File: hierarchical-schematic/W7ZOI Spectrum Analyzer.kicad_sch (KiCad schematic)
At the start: 2 parts

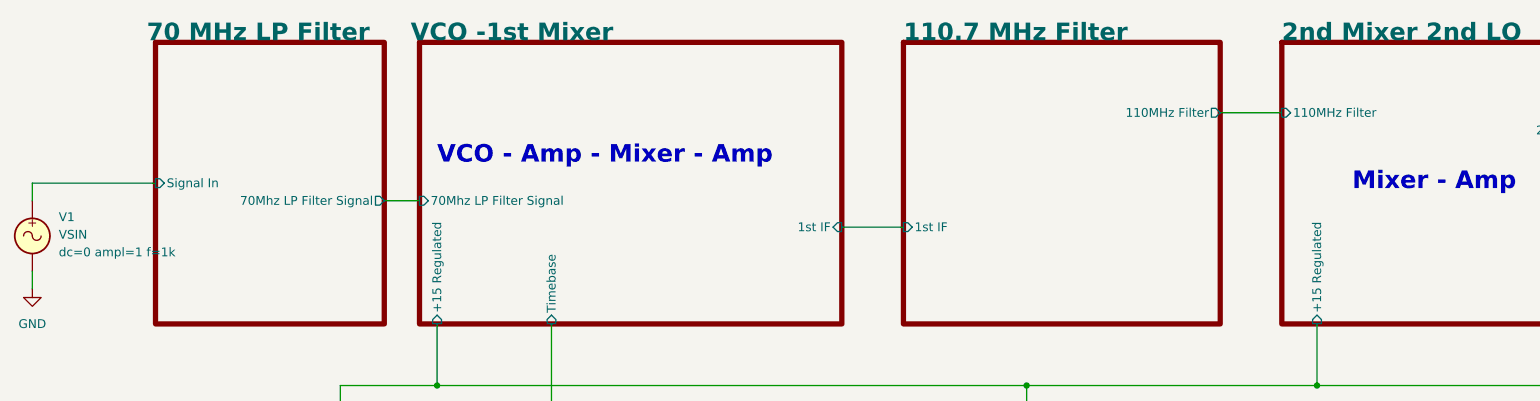
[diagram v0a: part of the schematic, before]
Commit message: Update to timebase and 2lo gerbers
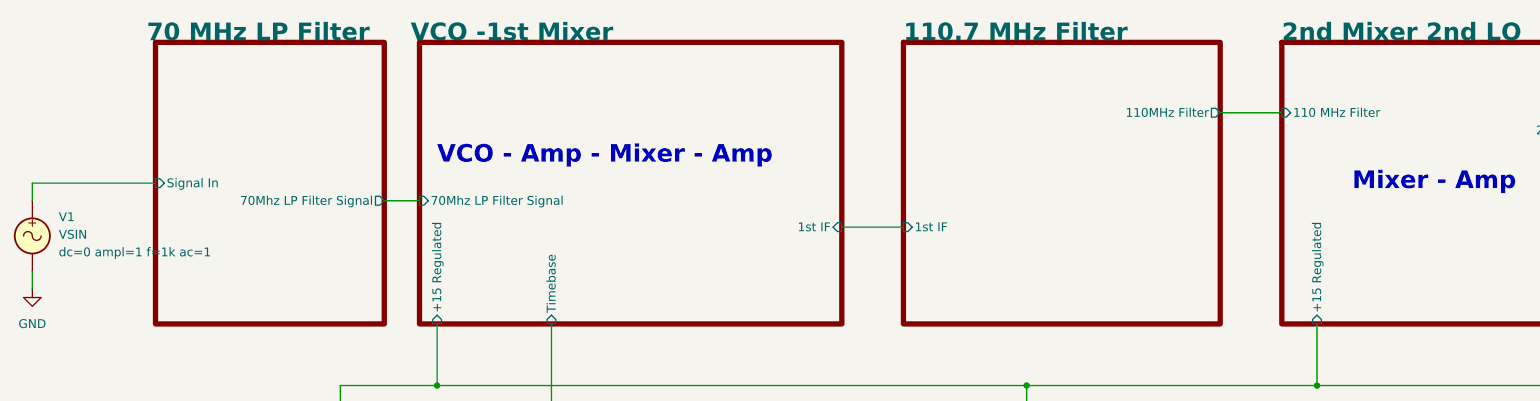
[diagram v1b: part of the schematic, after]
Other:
- sheet 2nd Mixer 2nd LO ports: added 110 MHz Filter; removed 110MHz Filter
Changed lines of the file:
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@@
       (effects (font (size 0 0)) hide)
     )
-    (property "Sim.Params" "dc=0 ampl=1 f=1k" (at 19.05 48.0701 0)
+    (property "Sim.Params" "dc=0 ampl=1 f=1k ac=1" (at 19.05 48.0701 0)
       (effects (font (size 1.27 1.27)) (justify left))
     )
@@
       (effects (font (size 1.27 1.27)) (justify left))
     )
-    (pin "110MHz Filter" input (at 195.58 27.94 180)
-      (effects (font (size 1.27 1.27)) (justify left))
-    )
     (pin "2nd Mixer" output (at 242.57 30.48 0)
       (effects (font (size 1.27 1.27)) (justify right))
     )
+    (pin "110 MHz Filter" input (at 195.58 27.94 180)
+      (effects (font (size 1.27 1.27)) (justify left))
+    )
     (instances

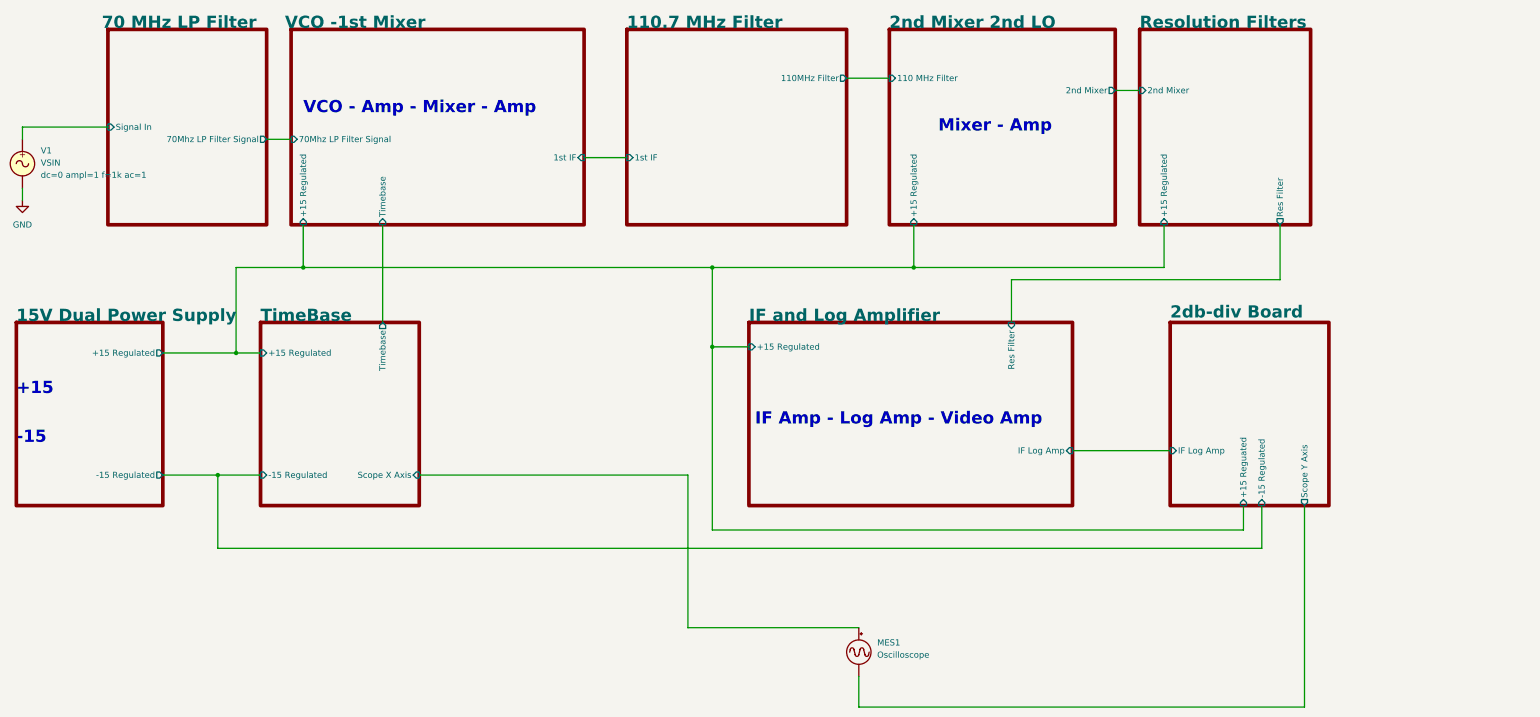
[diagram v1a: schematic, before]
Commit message: erc changes for hierarchical schematic
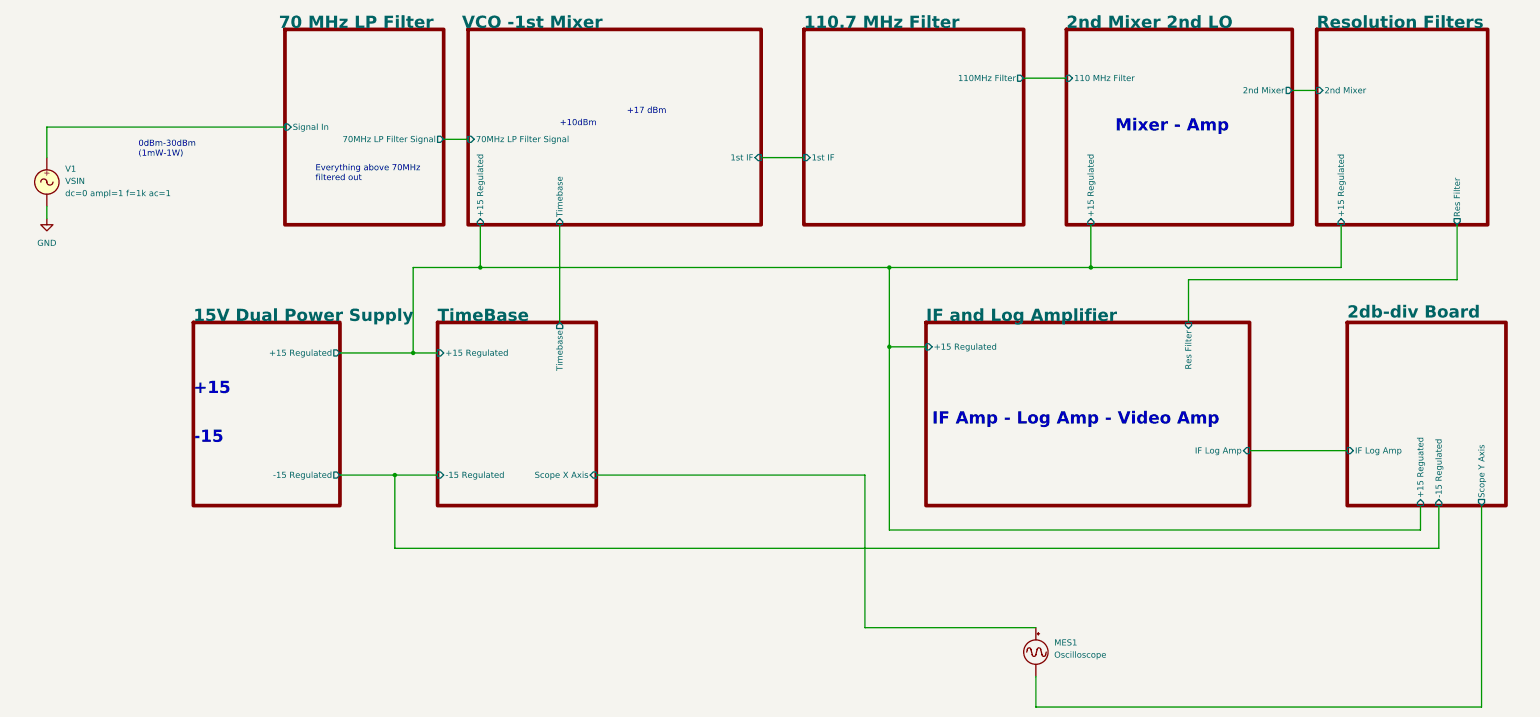
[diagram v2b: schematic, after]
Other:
- sheet 70 MHz LP Filter ports: added 70MHz LP Filter Signal; removed 70Mhz LP Filter Signal
- sheet VCO -1st Mixer ports: added 70MHz LP Filter Signal; removed 70Mhz LP Filter Signal
- note added: "+10dBm"
- note added: "+17 dBm"
- note added: "0dBm-30dBm (1mW-1W)"
- note added: "Everything above 70MHz filtered out"
- note removed: "VCO - Amp - Mixer - Amp"
- moved on the sheet: MES1, V1

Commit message: minor changes to multiple boards
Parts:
- added R2: 10k, symbol Device:R_Potentiometer_Trim_US
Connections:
- net 2db-div Board/IF Log Amp: now also R2.2
- net GND: now also R2.3
- new net IF and Log Amplifier/IF Log Amp: R2.1
